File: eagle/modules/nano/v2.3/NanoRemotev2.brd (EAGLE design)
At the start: 113 x 82.5 mm, 74 parts, among them IC1 ULN2803A, IC2 ULN2803A, IC4 ULN2803A, J1 RJ12STRAIGHT-RS232-SERVER

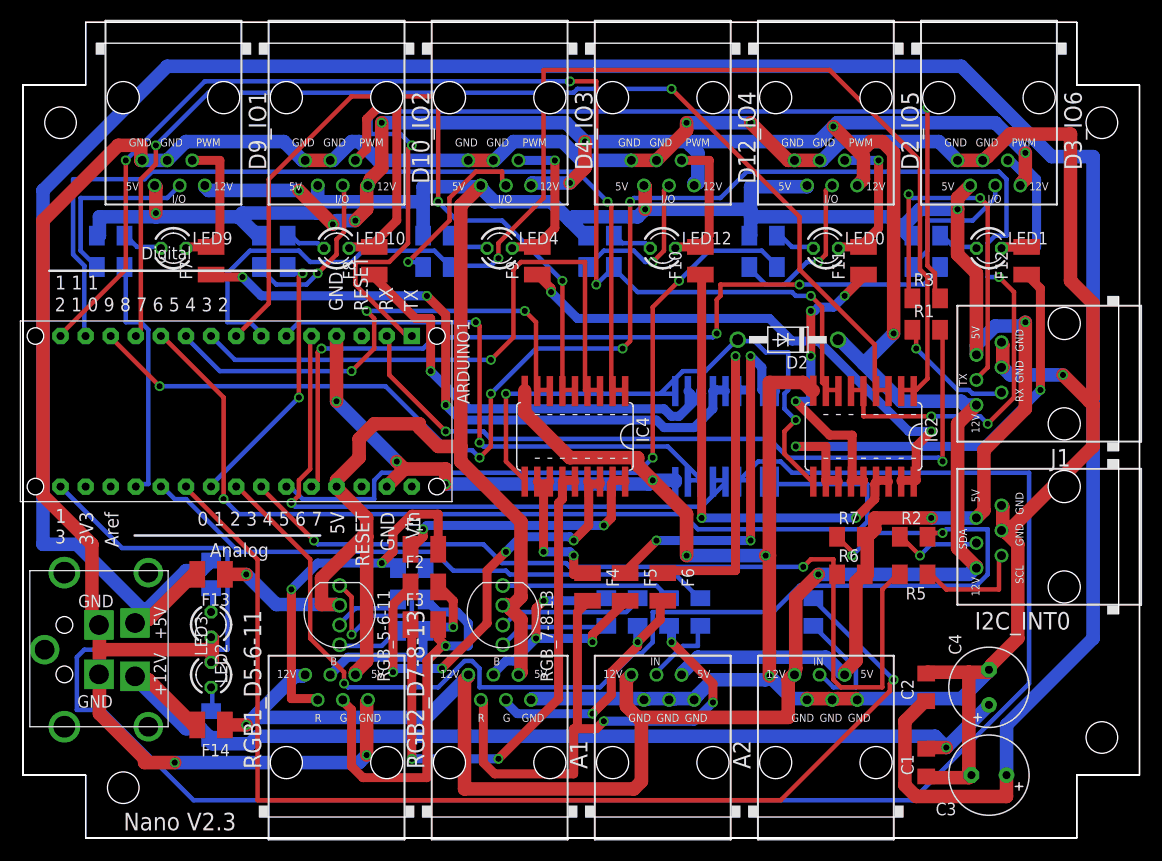
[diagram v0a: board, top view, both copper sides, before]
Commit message: Add led driver
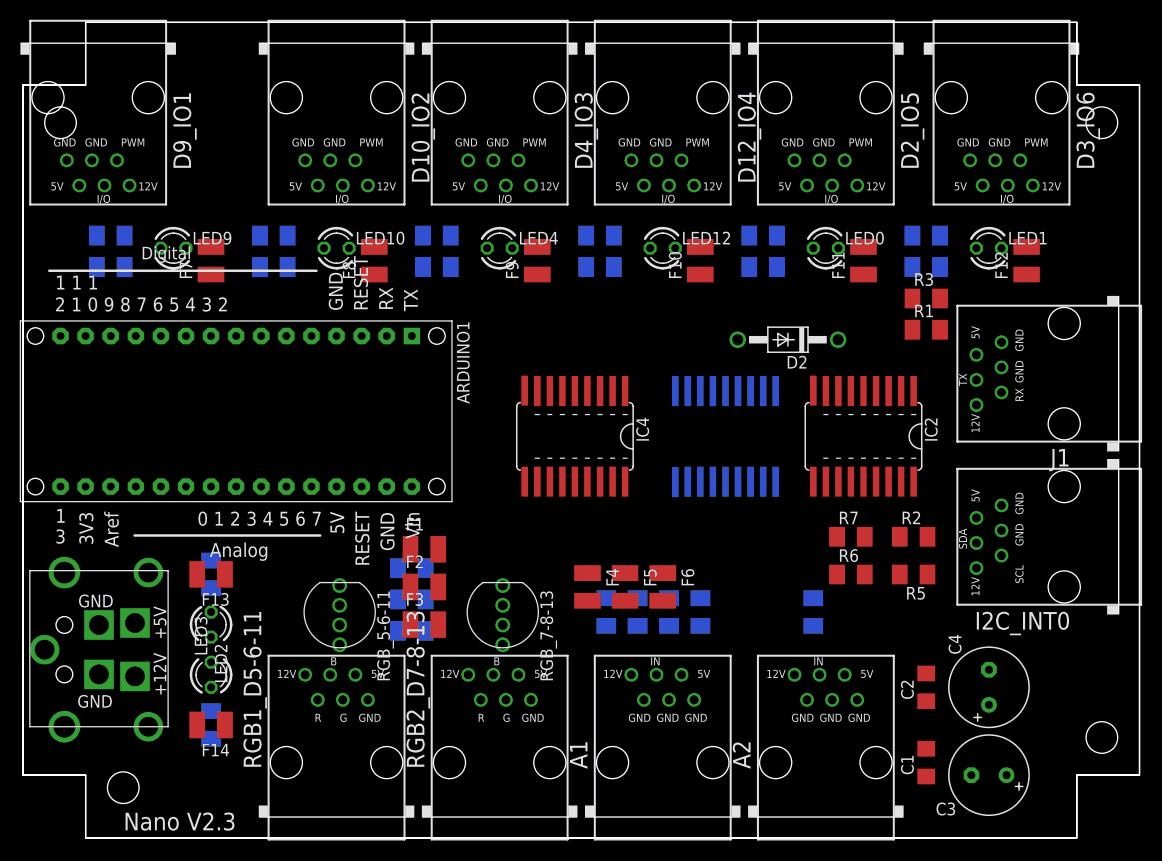
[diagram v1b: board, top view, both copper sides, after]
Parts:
- moved D9_IO1 7.62 mm to (6.35, 74.9)
- moved D3_IO6 1.27 mm to (97.8, 74.9)
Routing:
- net GND: track 488.7 -> 0.00 mm, vias 12 -> 0
- net +5V: track 334.3 -> 0.00 mm, vias 6 -> 0
- net +12V: track 305.4 -> 0.00 mm, vias 11 -> 0
- net N$37: track 272.7 -> 0.00 mm
- net D13: track 208.9 -> 0.00 mm
- net D10: track 165.5 -> 0.00 mm, vias 8 -> 0
- net D4: track 128.0 -> 0.00 mm, vias 1 -> 0
- net D12: track 127.3 -> 0.00 mm, vias 4 -> 0
- net SDA: track 123.5 -> 0.00 mm, vias 3 -> 0
- net A2: track 116.2 -> 0.00 mm, vias 1 -> 0
- net D9: track 115.2 -> 0.00 mm, vias 2 -> 0
- net TX: track 109.6 -> 0.00 mm, vias 2 -> 0
- net N$39: track 102.6 -> 0.00 mm, vias 1 -> 0
- net D8: track 100.5 -> 0.00 mm, vias 1 -> 0
- net D11: track 92.8 -> 0.00 mm, vias 1 -> 0
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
